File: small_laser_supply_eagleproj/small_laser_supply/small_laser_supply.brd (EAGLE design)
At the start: 55.9 x 25.4 mm, 24 parts, among them U1 LT6003_SOT23-5, X1 VIN, X2 CTRL, X3 OUT

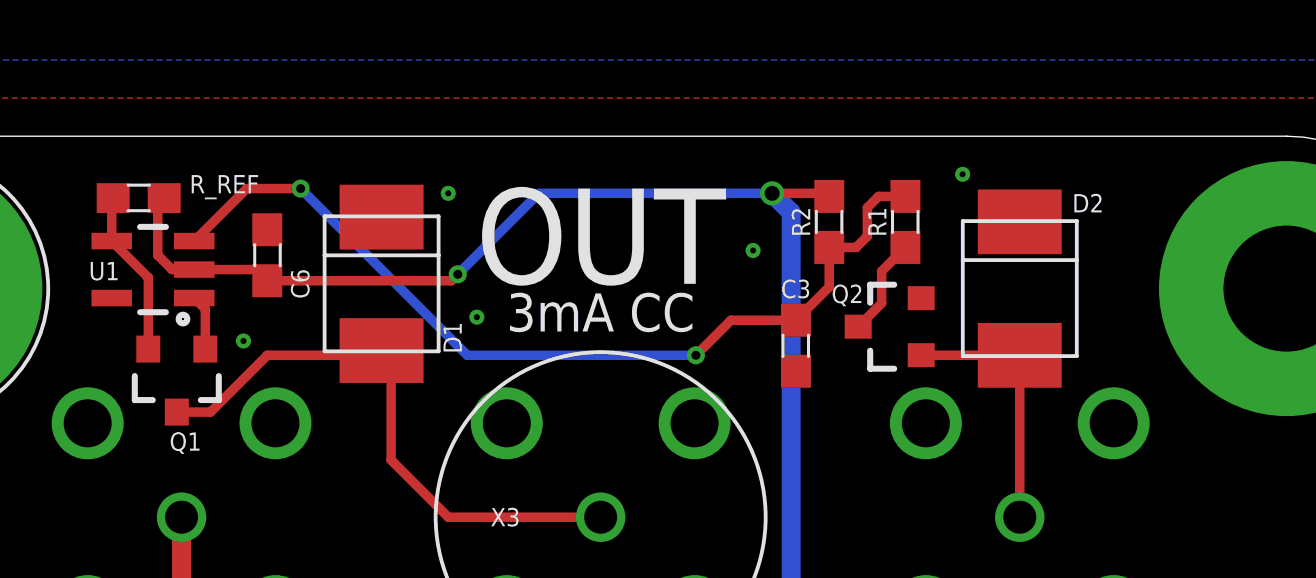
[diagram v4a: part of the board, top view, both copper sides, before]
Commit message: stuck a resistor across the pfet's gate last min, updated the board and images and gerbers and such
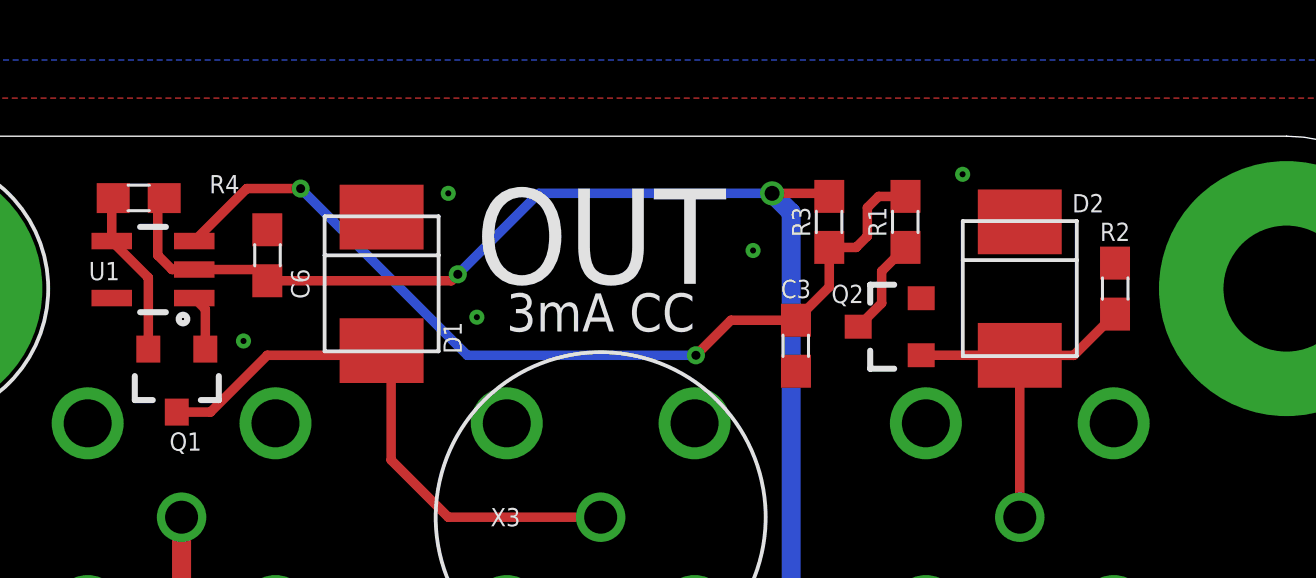
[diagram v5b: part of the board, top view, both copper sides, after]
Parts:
- added R3: 442, small_laser_supply_lib:0603
- R2: value 442 -> 4020
- moved R2 9.78 mm to (45.1, 20.3), turned to 270 degrees
- renumbered R_REF to R4
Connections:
- net -5V: now also R3.2; no longer R2.2
- net GND: now also R2.1
- net N$9: now also R2.2
- net V_REF: now also R3.1; no longer R2.1
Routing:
- net N$9: track 8.68 -> 12.4 mm
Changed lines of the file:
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@@
 <attribute name="NAME" x="11.90625" y="21.209" size="0.6096" layer="25" font="vector" ratio="16" rot="R180"/>
 </element>
-<element name="R_REF" library="small_laser_supply_lib" package="0603" value="165" x="12.54125" y="23.33625" smashed="yes">
+<element name="R4" library="small_laser_supply_lib" package="0603" value="165" x="12.54125" y="23.33625" smashed="yes">
 <attribute name="NAME" x="15.39875" y="23.495" size="0.6096" layer="25" font="vector" ratio="16" align="bottom-center"/>
 <attribute name="VALUE" x="15.08125" y="23.33625" size="0.6096" layer="27" font="vector" ratio="16" align="top-center"/>
@@
 <attribute name="VALUE" x="38.735" y="22.5425" size="0.6096" layer="27" font="vector" ratio="16" rot="R90" align="top-center"/>
 </element>
-<element name="R2" library="small_laser_supply_lib" package="0603" value="442" x="35.56" y="22.5425" smashed="yes" rot="R90">
+<element name="R3" library="small_laser_supply_lib" package="0603" value="442" x="35.56" y="22.5425" smashed="yes" rot="R90">
 <attribute name="NAME" x="34.925" y="22.5425" size="0.6096" layer="25" font="vector" ratio="16" rot="R90" align="bottom-center"/>
 <attribute name="VALUE" x="36.195" y="22.5425" size="0.6096" layer="27" font="vector" ratio="16" rot="R90" align="top-center"/>
@@
 <element name="D3" library="small_laser_supply_lib" package="DO-214AA" value="18v" x="21.59" y="5.08" rot="R90"/>
 <element name="PTC1" library="small_laser_supply_lib" package="2SMD_PTC" value="800mA" x="14.605" y="4.445"/>
+<element name="R2" library="small_laser_supply_lib" package="0603" value="4020" x="45.085" y="20.32" smashed="yes" rot="R270">
+<attribute name="NAME" x="45.085" y="21.9075" size="0.6096" layer="25" font="vector" ratio="16" align="bottom-center"/>
+<attribute name="VALUE" x="45.085" y="18.7325" size="0.6096" layer="27" font="vector" ratio="16" align="top-center"/>
+</element>
 </elements>
 <signals>
@@
 <via x="29.21" y="4.445" extent="1-16" drill="0.2"/>
 <via x="16.03375" y="18.57375" extent="1-16" drill="0.2"/>
+<contactref element="R2" pad="1"/>
 </signal>
 <signal name="-5V">
 <contactref element="U1" pad="2"/>
 <contactref element="C6" pad="2"/>
-<contactref element="R2" pad="2"/>
-<contactref element="R_REF" pad="2"/>
+<contactref element="R3" pad="2"/>
+<contactref element="R4" pad="2"/>
 <contactref element="VR1" pad="3"/>
 <contactref element="C2" pad="2"/>
@@
 </signal>
 <signal name="N$2">
-<contactref element="R_REF" pad="1"/>
+<contactref element="R4" pad="1"/>
 <contactref element="Q1" pad="2"/>
 <contactref element="U1" pad="4"/>
@@
 <signal name="V_REF">
 <contactref element="R1" pad="2"/>
-<contactref element="R2" pad="1"/>
+<contactref element="R3" pad="1"/>
 <contactref element="U1" pad="3"/>
 <contactref element="C3" pad="2"/>
@@
 <wire x1="41.91" y1="12.7" x2="41.91" y2="18.095" width="0.3175" layer="1"/>
 <wire x1="41.91" y1="18.095" x2="38.62375" y2="18.1" width="0.3175" layer="1"/>
+<contactref element="R2" pad="2"/>
+<wire x1="45.085" y1="19.47" x2="43.71" y2="18.095" width="0.3175" layer="1"/>
+<wire x1="43.71" y1="18.095" x2="41.91" y2="18.095" width="0.3175" layer="1"/>
 </signal>
 <signal name="N$3">
